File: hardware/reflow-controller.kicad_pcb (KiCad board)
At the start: 2 copper layers, 55.9 x 30.5 mm, 31 parts, among them J1 USB_B_Micro, J2 Conn_01x02, J3 Conn_02x03_Odd_Even, J4 Conn_01x02, J5 Conn_01x04, Q1 BC817, U1 MAX31855KASA, U2 AP2127K-3.3, U3 ATmega8U2-AU, Y1 8MHz

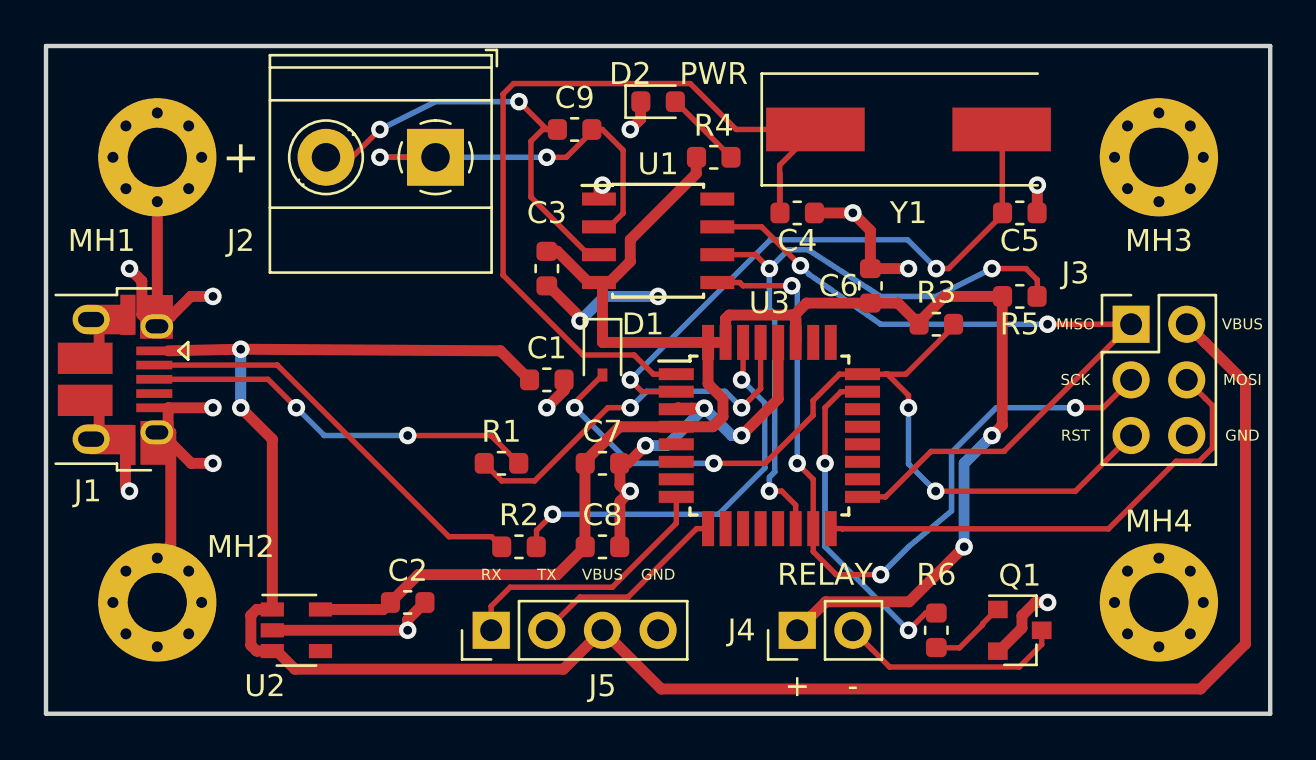
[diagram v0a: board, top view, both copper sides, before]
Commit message: Bom generation improvements.
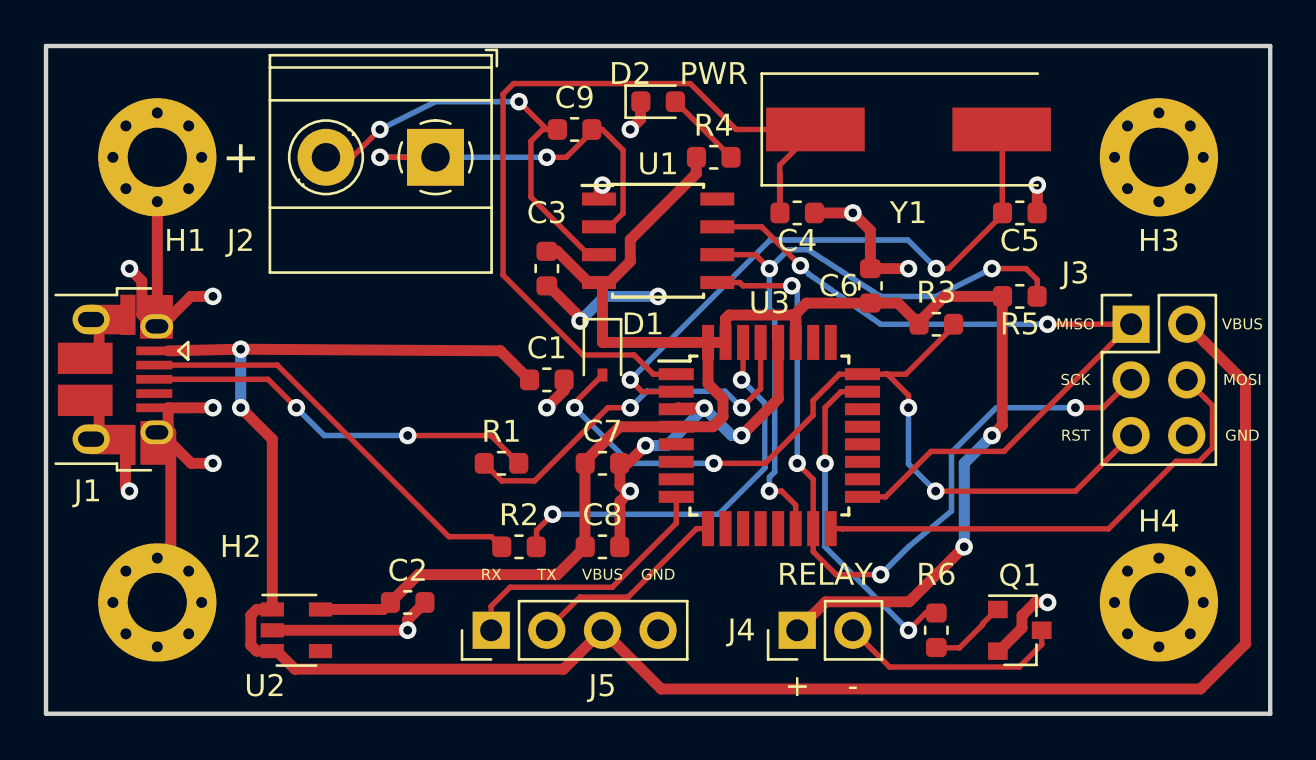
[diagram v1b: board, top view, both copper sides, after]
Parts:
- removed MH1, MH2, MH3, MH4: MountingHole_Pad, MountingHole:MountingHole_2.7mm_M2.5_Pad_Via
- added H1: MountingHole_Pad, MountingHole:MountingHole_2.7mm_M2.5_Pad_Via, F.Cu at (161.3, 52.1)
- added H2: MountingHole_Pad, MountingHole:MountingHole_2.7mm_M2.5_Pad_Via, F.Cu at (161.3, 72.4)
- added H3: MountingHole_Pad, MountingHole:MountingHole_2.7mm_M2.5_Pad_Via, F.Cu at (207.0, 52.1)
- added H4: MountingHole_Pad, MountingHole:MountingHole_2.7mm_M2.5_Pad_Via, F.Cu at (207.0, 72.4)
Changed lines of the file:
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@@
     )
-  )
-  (module MountingHole:MountingHole_2.7mm_M2.5_Pad_Via (layer F.Cu)
-    (at 161.29 52.07)
-    (descr "Mounting Hole 2.7mm")
-    (tags "mounting hole 2.7mm")
-    (attr virtual)
-    (fp_text reference MH1 (at -2.54 3.81) (layer F.SilkS)
-      (effects (font (size 1 1) (thickness 0.15)))
-    )
-    (fp_text value MountingHole_Pad (at 0 3.7) (layer F.Fab)
-      (effects (font (size 1 1) (thickness 0.15)))
-    )
-    (fp_text user %R (at 0.3 0) (layer F.Fab)
-      (effects (font (size 1 1) (thickness 0.15)))
-    )
-    (fp_circle (center 0 0) (end 2.7 0) (layer Cmts.User) (width 0.15))
-    (fp_circle (center 0 0) (end 2.95 0) (layer F.CrtYd) (width 0.05))
-    (pad 1 thru_hole circle (at 0 0) (size 5.4 5.4) (drill 2.7) (layers *.Cu *.Mask)
-      (net 1 GND))
-    (pad 1 thru_hole circle (at 2.025 0) (size 0.8 0.8) (drill 0.5) (layers *.Cu *.Mask)
-      (net 1 GND))
-    (pad 1 thru_hole circle (at 1.431891 1.431891) (size 0.8 0.8) (drill 0.5) (layers *.Cu *.Mask)
-      (net 1 GND))
-    (pad 1 thru_hole circle (at 0 2.025) (size 0.8 0.8) (drill 0.5) (layers *.Cu *.Mask)
-      (net 1 GND))
-    (pad 1 thru_hole circle (at -1.431891 1.431891) (size 0.8 0.8) (drill 0.5) (layers *.Cu *.Mask)
-      (net 1 GND))
-    (pad 1 thru_hole circle (at -2.025 0) (size 0.8 0.8) (drill 0.5) (layers *.Cu *.Mask)
-      (net 1 GND))
-    (pad 1 thru_hole circle (at -1.431891 -1.431891) (size 0.8 0.8) (drill 0.5) (layers *.Cu *.Mask)
-      (net 1 GND))
-    (pad 1 thru_hole circle (at 0 -2.025) (size 0.8 0.8) (drill 0.5) (layers *.Cu *.Mask)
-      (net 1 GND))
-    (pad 1 thru_hole circle (at 1.431891 -1.431891) (size 0.8 0.8) (drill 0.5) (layers *.Cu *.Mask)
-      (net 1 GND))
   )
   (module Connector_USB:USB_Micro-B_Amphenol_10103594-0001LF_Horizontal (layer F.Cu)
@@
   )
   (module MountingHole:MountingHole_2.7mm_M2.5_Pad_Via (layer F.Cu)
+    (at 161.29 52.07)
+    (descr "Mounting Hole 2.7mm")
+    (tags "mounting hole 2.7mm")
+    (attr virtual)
+    (fp_text reference H1 (at 1.27 3.81) (layer F.SilkS)
+      (effects (font (size 1 1) (thickness 0.15)))
+    )
+    (fp_text value MountingHole_Pad (at 0 3.7) (layer F.Fab)
+      (effects (font (size 1 1) (thickness 0.15)))
+    )
+    (fp_text user %R (at 0.3 0) (layer F.Fab)
+      (effects (font (size 1 1) (thickness 0.15)))
+    )
+    (fp_circle (center 0 0) (end 2.7 0) (layer Cmts.User) (width 0.15))
+    (fp_circle (center 0 0) (end 2.95 0) (layer F.CrtYd) (width 0.05))
+    (pad 1 thru_hole circle (at 0 0) (size 5.4 5.4) (drill 2.7) (layers *.Cu *.Mask)
+      (net 1 GND))
+    (pad 1 thru_hole circle (at 2.025 0) (size 0.8 0.8) (drill 0.5) (layers *.Cu *.Mask)
+      (net 1 GND))
+    (pad 1 thru_hole circle (at 1.431891 1.431891) (size 0.8 0.8) (drill 0.5) (layers *.Cu *.Mask)
+      (net 1 GND))
+    (pad 1 thru_hole circle (at 0 2.025) (size 0.8 0.8) (drill 0.5) (layers *.Cu *.Mask)
+      (net 1 GND))
+    (pad 1 thru_hole circle (at -1.431891 1.431891) (size 0.8 0.8) (drill 0.5) (layers *.Cu *.Mask)
+      (net 1 GND))
+    (pad 1 thru_hole circle (at -2.025 0) (size 0.8 0.8) (drill 0.5) (layers *.Cu *.Mask)
+      (net 1 GND))
+    (pad 1 thru_hole circle (at -1.431891 -1.431891) (size 0.8 0.8) (drill 0.5) (layers *.Cu *.Mask)
+      (net 1 GND))
+    (pad 1 thru_hole circle (at 0 -2.025) (size 0.8 0.8) (drill 0.5) (layers *.Cu *.Mask)
+      (net 1 GND))
+    (pad 1 thru_hole circle (at 1.431891 -1.431891) (size 0.8 0.8) (drill 0.5) (layers *.Cu *.Mask)
+      (net 1 GND))
+  )
+  (module MountingHole:MountingHole_2.7mm_M2.5_Pad_Via (layer F.Cu)
     (at 161.29 72.39)
     (descr "Mounting Hole 2.7mm")
     (tags "mounting hole 2.7mm")
     (attr virtual)
-    (fp_text reference MH2 (at 3.81 -2.54) (layer F.SilkS)
+    (fp_text reference H2 (at 3.81 -2.54) (layer F.SilkS)
       (effects (font (size 1 1) (thickness 0.15)))
     )
@@
     (tags "mounting hole 2.7mm")
     (attr virtual)
-    (fp_text reference MH3 (at 0 3.81) (layer F.SilkS)
+    (fp_text reference H3 (at 0 3.81) (layer F.SilkS)
       (effects (font (size 1 1) (thickness 0.15)))
     )
@@
     (tags "mounting hole 2.7mm")
     (attr virtual)
-    (fp_text reference MH4 (at 0 -3.7) (layer F.SilkS)
-      (effects (font (size 1 1) (thickness 0.15)))
-    )
+    (fp_text reference H4 (at 0 -3.7) (layer F.SilkS)
+      (effects (font (size 1 1) (thickness 0.15)))
+    )
